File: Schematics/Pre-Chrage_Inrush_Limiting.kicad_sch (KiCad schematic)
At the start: 0 parts

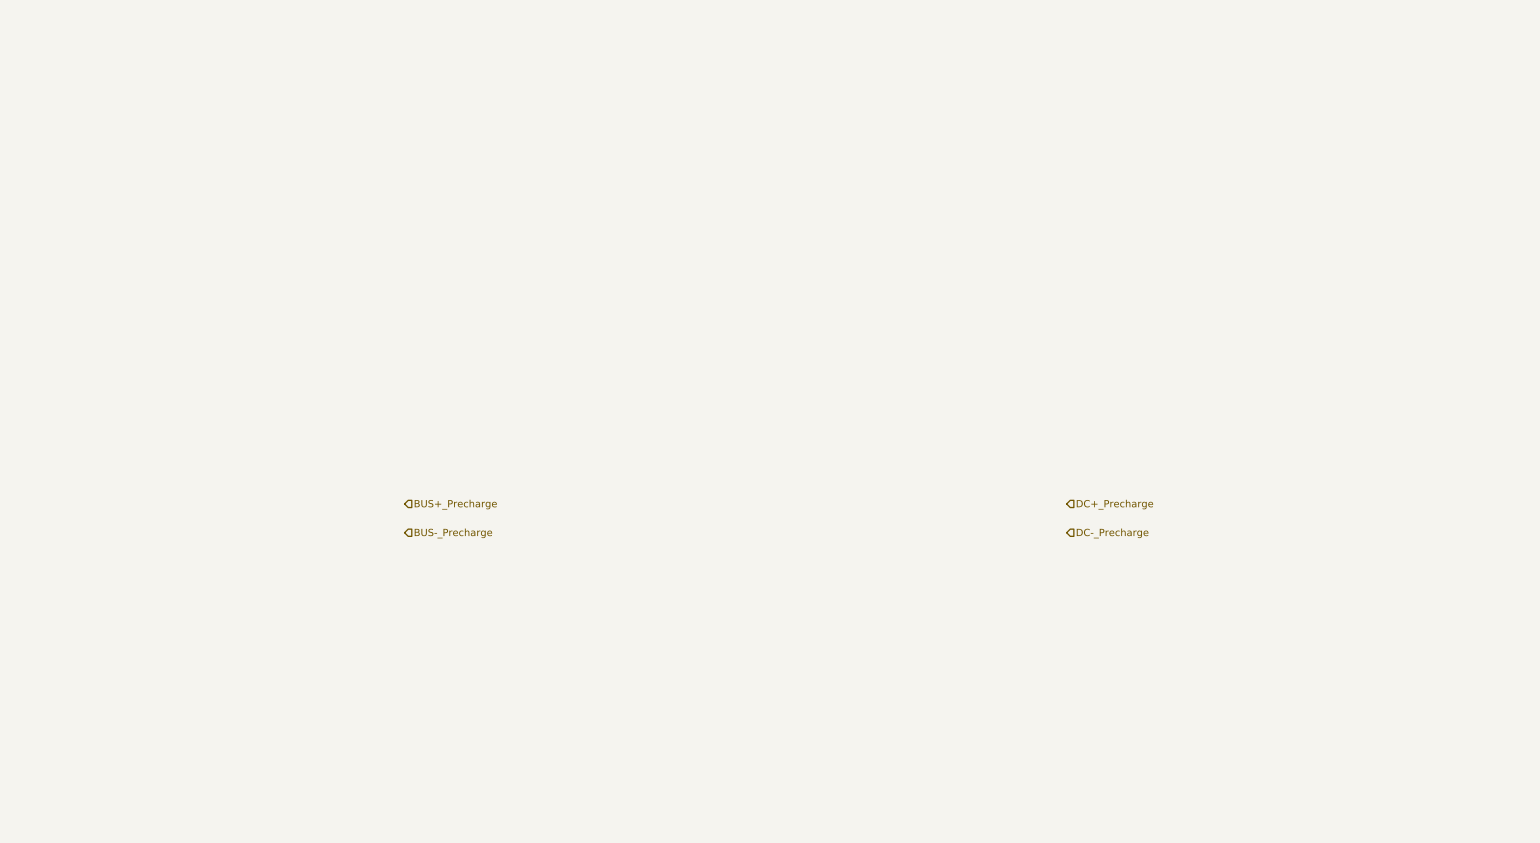
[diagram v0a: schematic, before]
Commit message: [WIP - SIC Inverter]
- Added 3d models for 3 parts
- Added 3 new footprints for the 3 added parts
- Changed footprint 23AH8785 and 86 Black and Red
- Finished WIP with EMI, Input Protection, and Precharge
- Added datasheet
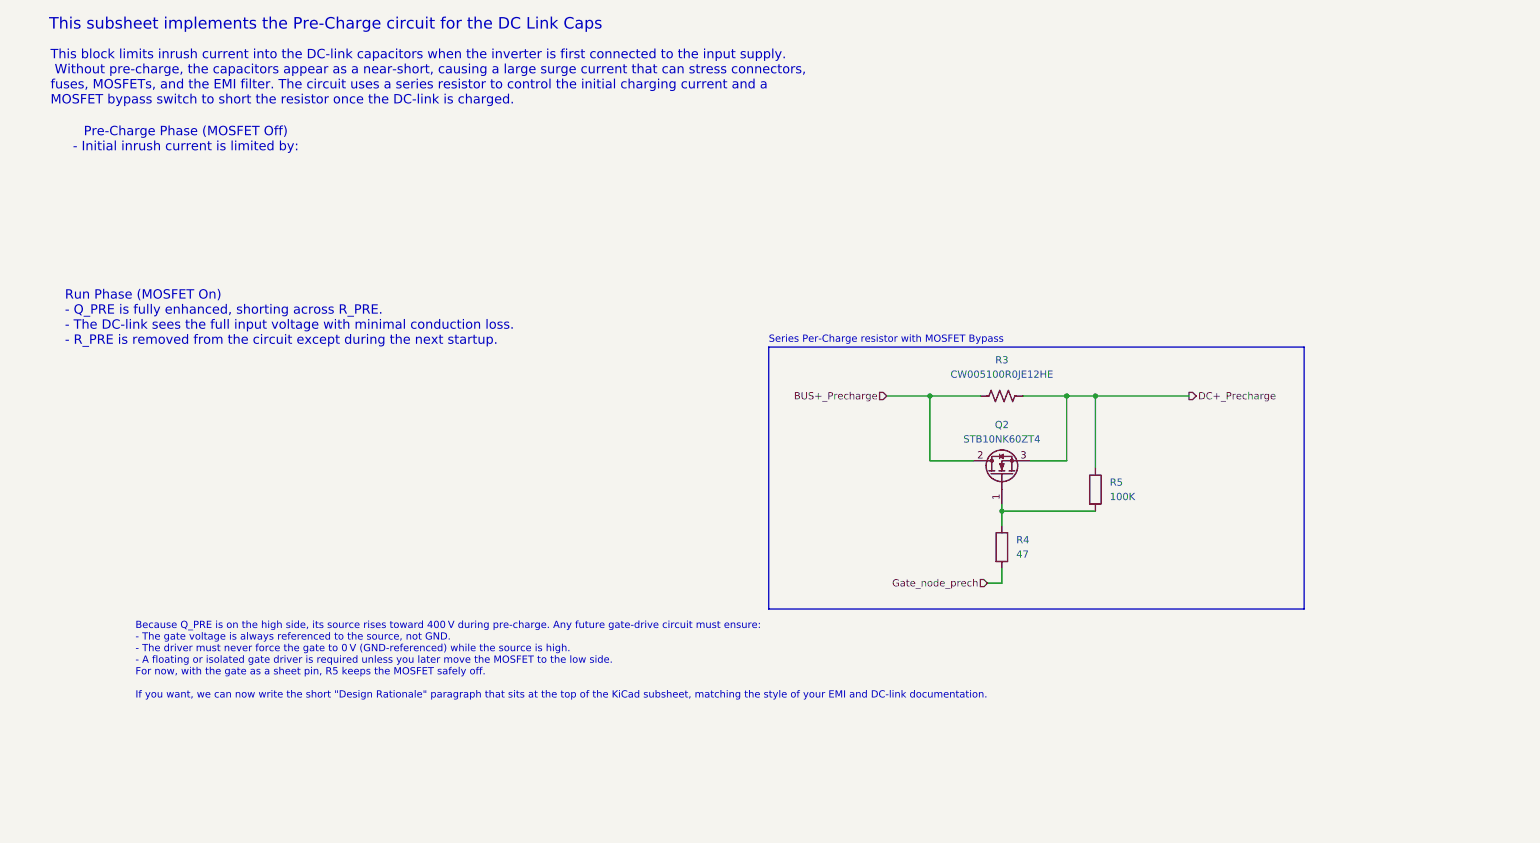
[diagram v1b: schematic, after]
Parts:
- added Q2: STB10NK60ZT4, Package_TO_SOT_SMD:TO-263-2, symbol SiC_Inverter:STB10NK60ZT4
- added R3: CW005100R0JE12HE, SiC_Inverter:CW005100R0JE12HE, symbol SiC_Inverter:CW005100R0JE12HE
- added R4: 47, Resistor_SMD:R_1206_3216Metric, symbol Device:R
- added R5: 100K, Resistor_SMD:R_1206_3216Metric, symbol Device:R
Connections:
- net BUS+_Precharge: now also Q2.2, R3.1
- net DC+_Precharge: now also Q2.3, R3.2, R5.1
- new net: Q2.1 (G), R4.1, R5.2
- new net Gate_node_prech: R4.2
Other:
- note added: "Because Q_PRE is on the high side, its source rises toward 400 V during pre‑charge. Any future gate‑drive circuit must ensure: - The gate voltage is always referenced to the source, not GND. - The driver must never force the gate to 0 V (GND‑referenced) while the source is high. - A floating or isolated gate driver is required unless you later move the MOSFET to the low side. For now, with the ga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"
- note added: "Pre‑Charge Phase (MOSFET Off) - Initial inrush current is limited by:"
- note added: "Run Phase (MOSFET On) - Q_PRE is fully enhanced, shorting across R_PRE. - The DC‑link sees the full input voltage with minimal conduction loss. - R_PRE is removed from the circuit except during the next startup."
- note added: "Series Per-Charge resistor with MOSFET Bypass"
- note added: "This block limits inrush current into the DC‑link capacitors when the inverter is first connected to the input supply. Without pre‑charge, the capacitors appear as a near‑short, causing a large surge current that can stress connectors, fuses, MOSFETs, and the EMI filter. The circuit uses a series resistor to control the initial charging current and a MOSFET bypass switch to short the resistor onc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"
- note added: "This subsheet implements the Pre-Charge circuit for the DC Link Caps"

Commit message: [WIP Full Bridge Leg A High Side]
- Changed Footprint for Black and Red connectors to THP but no Pin
  number
- Changed DC Link cap sub sheet to have a cleaner look
- Change footprint in 1206 reister to head solder pads
- WIP Full Bridge Leg A High Side
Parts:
- R4, R5: footprint Resistor_SMD:R_1206_3216Metric -> Resistor_SMD:R_1206_3216Metric_Pad1.30x1.75mm_HandSolder
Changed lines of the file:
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@@
 			)
 		)
-		(property "Footprint" "Resistor_SMD:R_1206_3216Metric"
+		(property "Footprint" "Resistor_SMD:R_1206_3216Metric_Pad1.30x1.75mm_HandSolder"
 			(at 179.832 107.95 90)
 			(effects
@@
 			)
 		)
-		(property "Footprint" "Resistor_SMD:R_1206_3216Metric"
+		(property "Footprint" "Resistor_SMD:R_1206_3216Metric_Pad1.30x1.75mm_HandSolder"
 			(at 196.342 97.79 90)
 			(effects

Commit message: Changing Text to Text Block
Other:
- note removed: "Series Per-Charge resistor with MOSFET Bypass"
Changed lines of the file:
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@@
-		)
-	)
-	(text "Series Per-Charge resistor with MOSFET Bypass"
-		(exclude_from_sim no)
-		(at 140.462 71.374 0)
-		(effects
-			(font
-				(size 1.27 1.27)
-			)
-			(justify left)
 		)
 	)
@@
 		)
 	)
+	(text_box "Series Per-Charge resistor with MOSFET Bypass"
+		(exclude_from_sim no)
+		(at 140.462 69.342 0)
+		(size 49.276 3.048)
+		(margins 0.9525 0.9525 0.9525 0.9525)
+		(stroke
+			(width 0)
+			(type solid)
+		)
+		(fill
+			(type color)
+			(color 0 0 255 0.1)
+		)
+		(effects
+			(font
+				(size 1.27 1.27)
+			)
+			(justify left top)
+		)
+	)

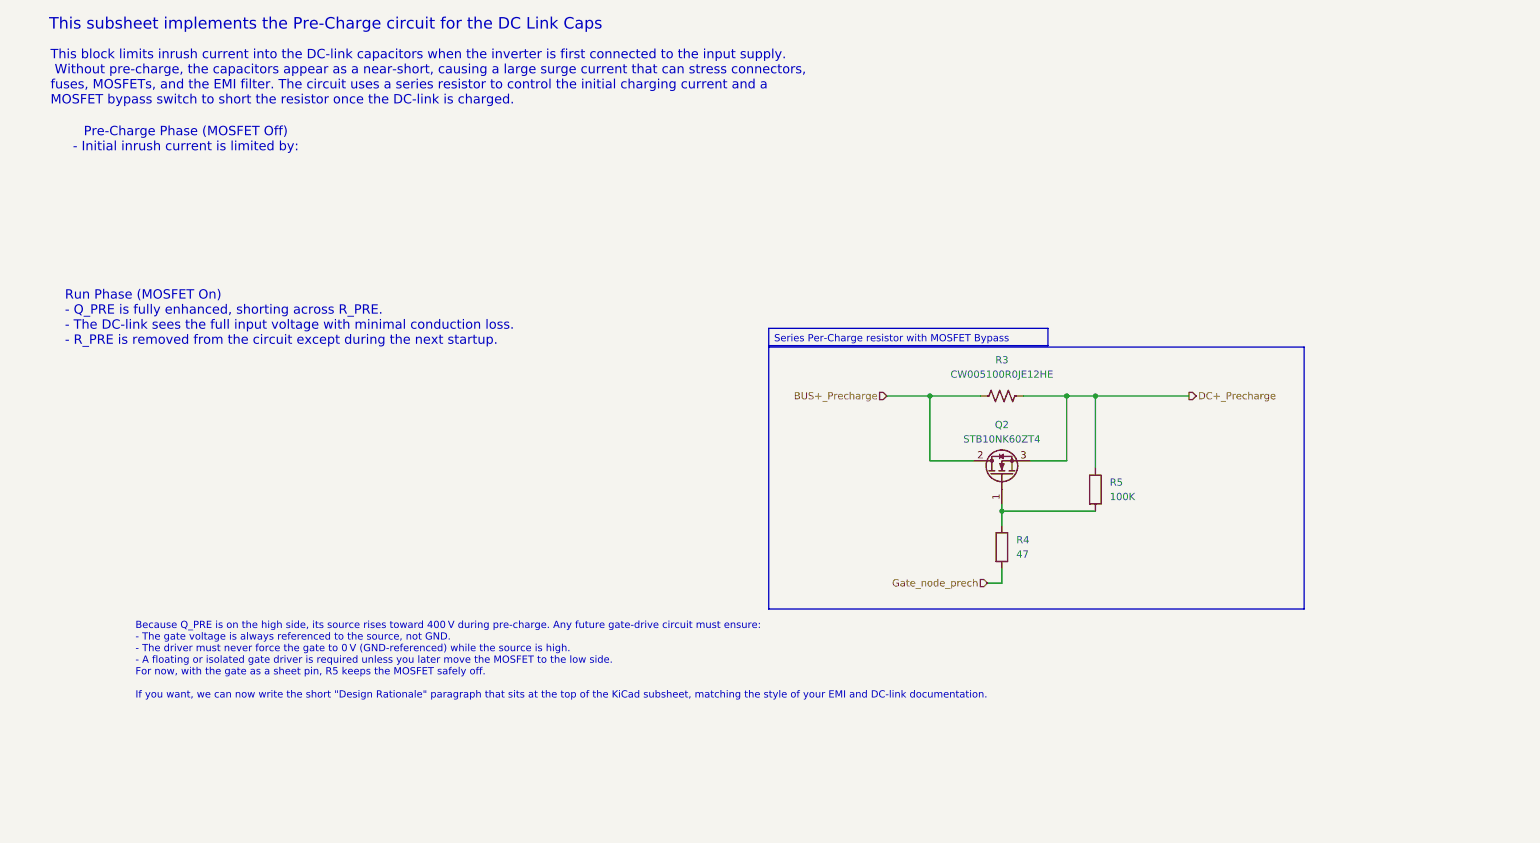
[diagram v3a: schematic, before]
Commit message: [WIP Single Phase SiC Inverter]
- Added molex 4 pin pcb connector for +15V power
- Added 3d model, symbol and footprint
- Added datasheet for molex connector
- Added Male and Female pcb - pcb connectors to all sub sheets
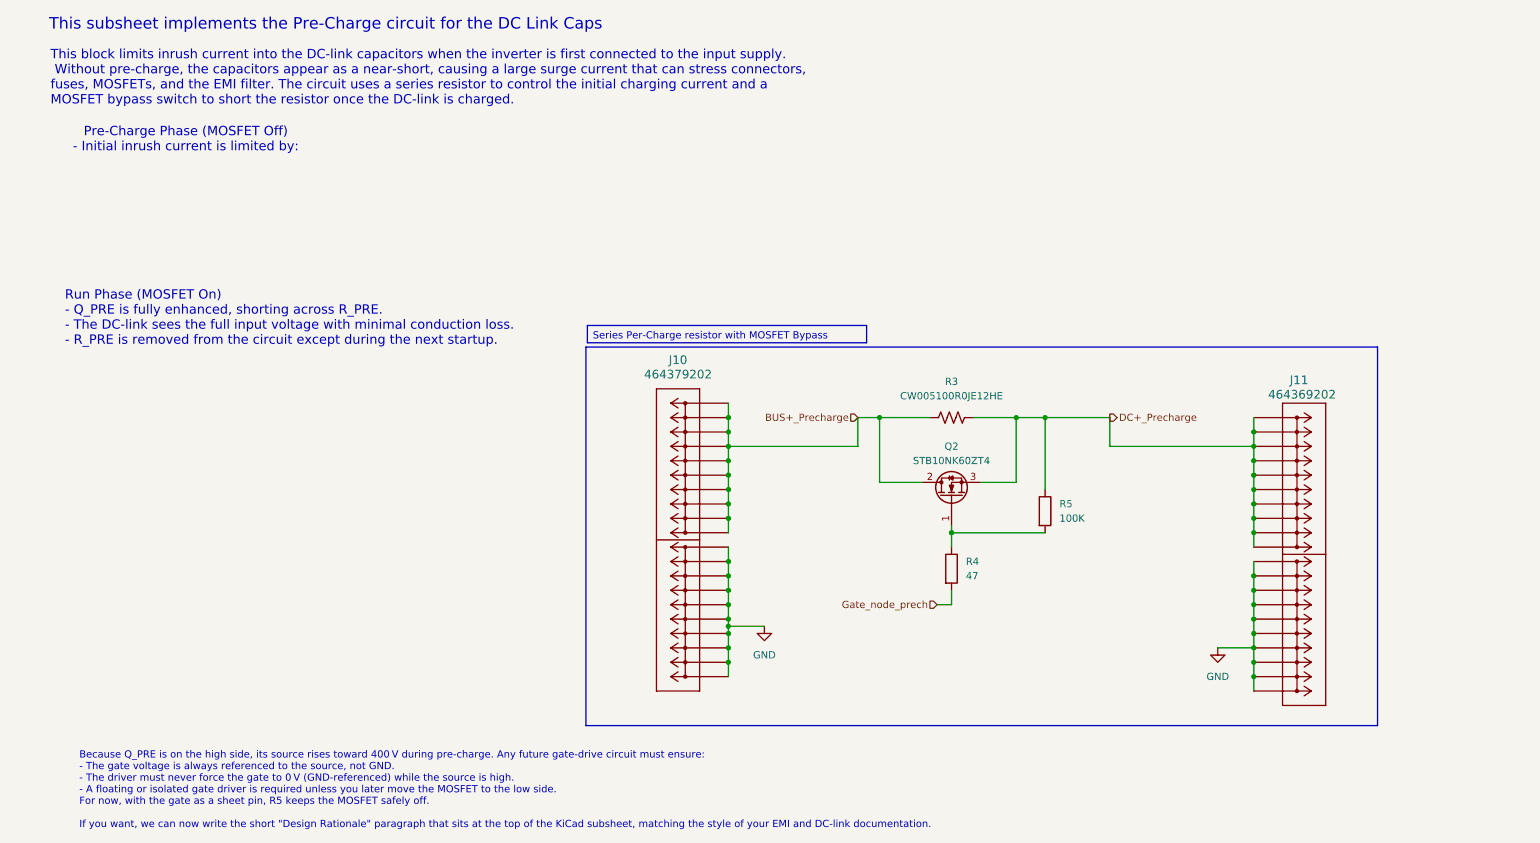
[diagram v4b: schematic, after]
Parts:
- added J10: 464379202, SiC_Inverter:46437-900_02, symbol SiC_Inverter:464379202
- added J11: 464369202, SiC_Inverter:46436-900_02, symbol SiC_Inverter:464369202
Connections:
- net BUS+_Precharge: now also J10.P2_1, J10.P2_10, J10.P2_2, J10.P2_3, J10.P2_4, J10.P2_5, J10.P2_6, J10.P2_7, J10.P2_8, J10.P2_9
- net DC+_Precharge: now also J11.P1_1, J11.P1_10, J11.P1_2, J11.P1_3, J11.P1_4, J11.P1_5, J11.P1_6, J11.P1_7, J11.P1_8, J11.P1_9
- new net GND: J10.P1_1, J10.P1_10, J10.P1_2, J10.P1_3, J10.P1_4, J10.P1_5, J10.P1_6, J10.P1_7, J10.P1_8, J10.P1_9, J11.P2_1, J11.P2_10, J11.P2_2, J11.P2_3, J11.P2_4, J11.P2_5, J11.P2_6, J11.P2_7, J11.P2_8, J11.P2_9
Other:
- moved on the sheet: Q2, R3, R4, R5

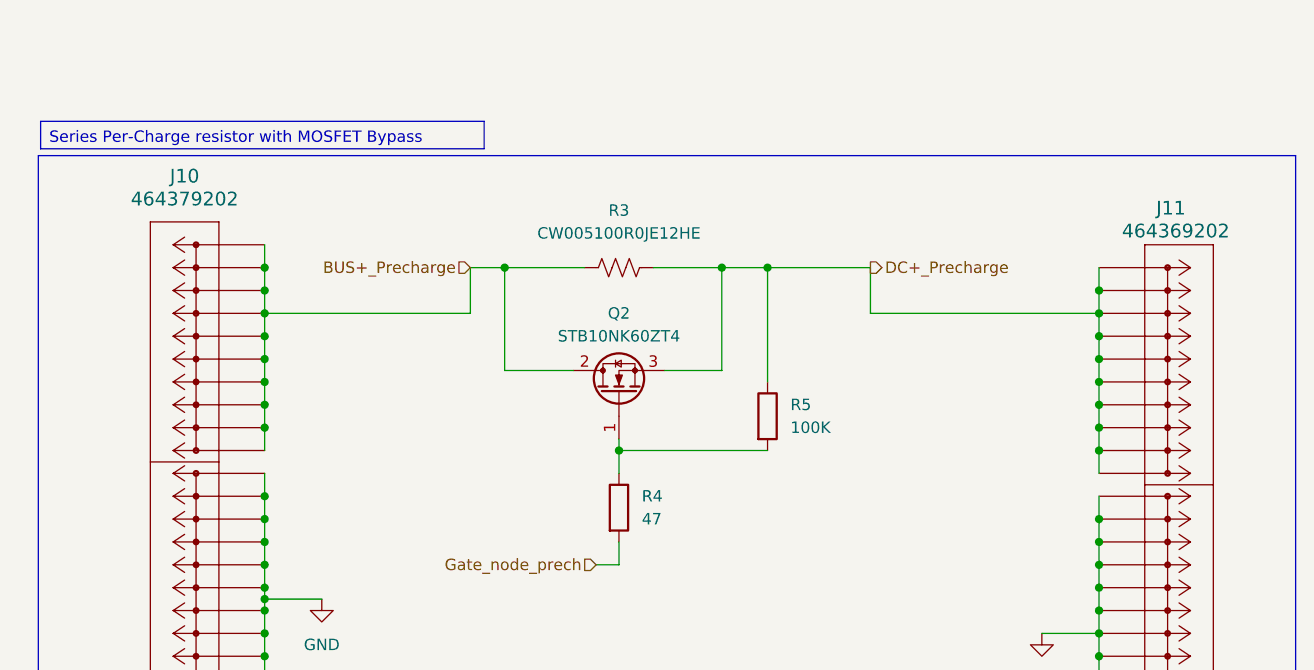
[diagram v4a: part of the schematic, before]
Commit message: [WIP Single Phase Inverter]
- Changed all Refs within each sub sheet (Stripe)
- Added 3V3 Power Supply off of 15V iso supply
- Added footprint, symbol and 3d part
- updated PCB with new part
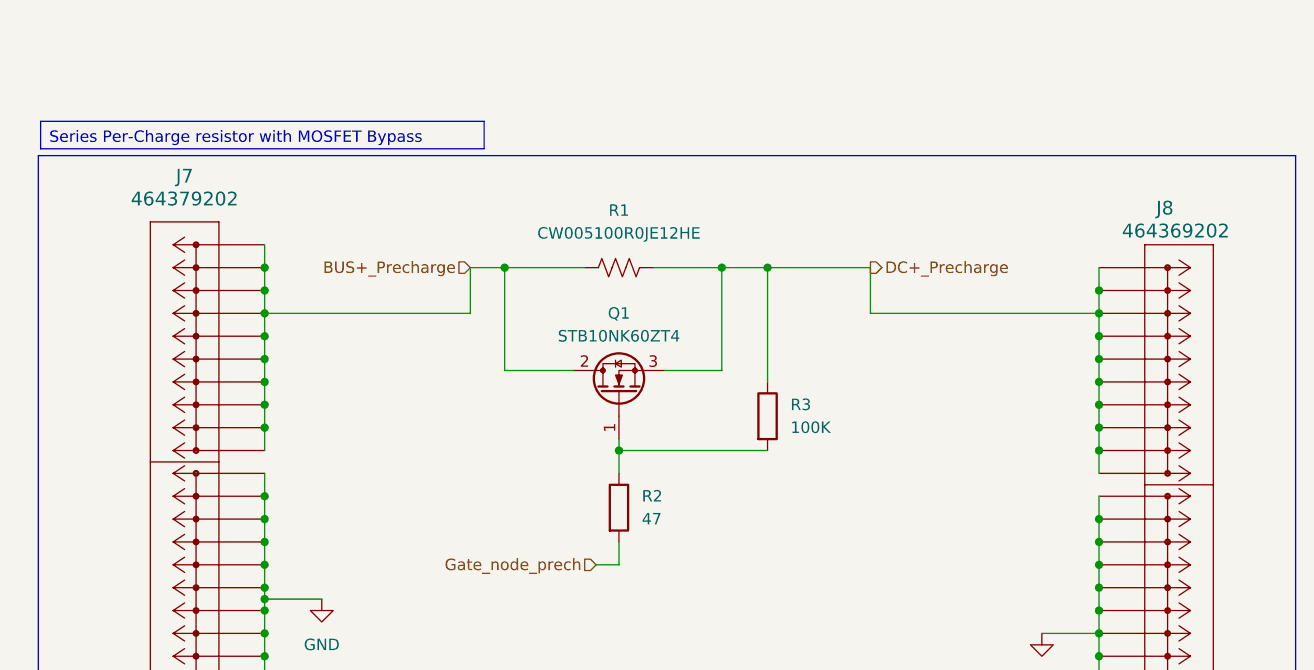
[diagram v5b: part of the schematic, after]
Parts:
- renumbered J10 to J7, J11 to J8, Q2 to Q1, R3 to R1, R4 to R2, R5 to R3
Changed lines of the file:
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@@
 		(on_board yes)
 		(dnp no)
-		(property "Reference" "J11"
+		(property "Reference" "J8"
 			(at 232.41 78.486 0)
 			(effects
@@
 			(project "SiC_Single_Phase_Inverter"
 				(path "/a1ed0539-9735-4ad1-a8fd-87e26e7fce16/2ce2cec5-32d3-4a43-a037-f5e3105f4dec"
-					(reference "J11")
+					(reference "J8")
 					(unit 1)
 				)
@@
 		(dnp no)
 		(fields_autoplaced yes)
-		(property "Reference" "R4"
+		(property "Reference" "R2"
 			(at 175.26 110.4899 0)
 			(effects
@@
 			(project "SiC_Single_Phase_Inverter"
 				(path "/a1ed0539-9735-4ad1-a8fd-87e26e7fce16/2ce2cec5-32d3-4a43-a037-f5e3105f4dec"
-					(reference "R4")
+					(reference "R2")
 					(unit 1)
 				)
@@
 		(dnp no)
 		(fields_autoplaced yes)
-		(property "Reference" "#PWR089"
+		(property "Reference" "#PWR06"
 			(at 219.71 132.08 0)
 			(effects
@@
 			(project "SiC_Single_Phase_Inverter"
 				(path "/a1ed0539-9735-4ad1-a8fd-87e26e7fce16/2ce2cec5-32d3-4a43-a037-f5e3105f4dec"
-					(reference "#PWR089")
+					(reference "#PWR06")
 					(unit 1)
 				)
@@
 		(dnp no)
 		(fields_autoplaced yes)
-		(property "Reference" "R5"
+		(property "Reference" "R3"
 			(at 191.77 100.3299 0)
 			(effects
@@
 			(project "SiC_Single_Phase_Inverter"
 				(path "/a1ed0539-9735-4ad1-a8fd-87e26e7fce16/2ce2cec5-32d3-4a43-a037-f5e3105f4dec"
-					(reference "R5")
+					(reference "R3")
 					(unit 1)
 				)
@@
 		(dnp no)
 		(fields_autoplaced yes)
-		(property "Reference" "J10"
+		(property "Reference" "J7"
 			(at 124.46 74.93 0)
 			(effects
@@
 			(project "SiC_Single_Phase_Inverter"
 				(path "/a1ed0539-9735-4ad1-a8fd-87e26e7fce16/2ce2cec5-32d3-4a43-a037-f5e3105f4dec"
-					(reference "J10")
+					(reference "J7")
 					(unit 1)
 				)
@@
 		(dnp no)
 		(fields_autoplaced yes)
-		(property "Reference" "#PWR088"
+		(property "Reference" "#PWR05"
 			(at 139.7 128.27 0)
 			(effects
@@
 			(project "SiC_Single_Phase_Inverter"
 				(path "/a1ed0539-9735-4ad1-a8fd-87e26e7fce16/2ce2cec5-32d3-4a43-a037-f5e3105f4dec"
-					(reference "#PWR088")
+					(reference "#PWR05")
 					(unit 1)
 				)
@@
 		(dnp no)
 		(fields_autoplaced yes)
-		(property "Reference" "R3"
+		(property "Reference" "R1"
 			(at 172.72 78.74 90)
 			(effects
@@
 			(project ""
 				(path "/a1ed0539-9735-4ad1-a8fd-87e26e7fce16/2ce2cec5-32d3-4a43-a037-f5e3105f4dec"
-					(reference "R3")
+					(reference "R1")
 					(unit 1)
 				)
@@
 		(dnp no)
 		(fields_autoplaced yes)
-		(property "Reference" "Q2"
+		(property "Reference" "Q1"
 			(at 172.72 90.17 90)
 			(effects
@@
 			(project ""
 				(path "/a1ed0539-9735-4ad1-a8fd-87e26e7fce16/2ce2cec5-32d3-4a43-a037-f5e3105f4dec"
-					(reference "Q2")
-					(unit 1)
-				)
+					(reference "Q1")
+					(unit 1)
+				)
